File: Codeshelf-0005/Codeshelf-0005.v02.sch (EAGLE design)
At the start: 26 parts, among them J1 RJ45-8PTH, J2 RJ45-8PTH, U2 MC9S08QG-DT, U3 CAT9552, U4 RS485SOIC, U7 7SEGMENT-2DIGIT

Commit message: Changes related to design review with Ravi and Charlie.
Mainly we need a new way to connect all of the boards where the cables
enter the back.
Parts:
- removed ACK.BUTTON.KEYCAP, CASE, STANDOFF1, STANDOFF2, STANDOFF3, STANDOFF4: EXTERNAL-COMPONENT, GW-devices:EXTERNAL-COMPONENT
- removed BDM: HEADER-3X2, GW-devices:HEADER-3X2
- removed R.D2A, R.D2B, R.D2C, R.D2D: RESISTOR-ARRAY-4X-3216, GW-devices:RESISTOR-ARRAY-4X-3216
- removed SW-ACK: SWITCH-TACTILE-320.03E11, GW-devices:SWITCH-TACTILE-320.03E11
- removed SW-DEC, SW-INC: SWITCH-TACTILE-FSM, GW-devices:SWITCH-TACTILE-FSM
- removed U7: 7SEGMENT-2DIGIT, GW-devices:7SEGMENT-2DIGIT
- added C10: 10uF, SparkFun:CAP_POL1206
- added C11: 68uF, SparkFun:CAP_POL3528
- added C3, C4: 100pF, GW-devices:RF-C0603
- added C5, C6, C7, C8, C9: .1uF, GW-devices:RF-C0402
- added CCOMP: 68pF, GW-devices:RF-C0805
- added CIN: 47uF, GW-devices:RF-C1210
- added COUT1: 100uF, GW-devices:RF-C1210
- added CSS: 2.7nF, GW-devices:RF-C0805
- added D1: RED, led:LEDCHIP-LED0805
- added D2: GREEN, led:LEDCHIP-LED0805
- added D3: MBRA140, SparkFun:DIODESMA
- added J3-WAKE: M02PTH, SparkFun-Connectors:M02PTH
- added J4: RJ45-8PTH, SparkFun:RJ45-8PTH
- added J5: HEADER-2X-2.54MM, GW-devices:HEADER-2X-2.54MM
- added J5-LCD-3V3, J6-LCD-5V: (no value), SparkFun-Connectors:M03PTH
- added JF1, JF2: JUMPER-2X-SMT-VIA, GW-devices:JUMPER-2X-SMT-VIA
- added L1: 150uH, GW-devices:INDUCTOR-SMD-UNUSUAL-SLF10165
- added L2: 47uH, SparkFun:INDUCTORCR54
- added LCD: LCD-SPARKFUN, GW-devices:LCD-SPARKFUN20X4
- added LED-ACTION: LED5060A, GW-devices:LED5060A
- added R-T: 120, GW-devices:RF-R0402
- added R.ACT.B, R.ACT.G: 10, GW-devices:RF-R0402
- added R.ACT.R: 68, GW-devices:RF-R0402
- added RCOMP: 4.64K, GW-devices:RF-R0402
- added REN1: 22K, GW-devices:RF-R0402
- added REN2: 10K, GW-devices:RF-R0402
- added RFB1: 45.3K, GW-devices:RF-R0402
- added RFB2: 143K, GW-devices:RF-R0402
- added U-P1: LM2854MH, GW-devices:LM2854MH
- added U-P2: PCHANNEL-MOSFET-DPAK, GW-devices:PCHANNEL-MOSFET-DPAK
- added U-P3: NCP1402, SparkFun:V_REG_NCP1400SOT23-5
- added U1: ZSFM201-1A, GW-devices:ZSFM201-1A
- added U5, U6: MIC94061C6, GW-devices:MIC94061C6
- C1: value .1uF -> 100pF; device GW-devices:RF-C0402 -> GW-devices:RF-C0603; MFGP GRM033R61A104KE15D -> C0603C101K5RACTU; PRICE 0.02 -> (none)
- C2: value .1uF -> 1nF; device GW-devices:RF-C0402 -> GW-devices:RF-C0603; MFGP GRM033R61A104KE15D -> C0603C102K4RACTU; PRICE 0.02 -> (none)
- J1: value RJ45-8PTH -> M05X2PTH; device GW-devices:RJ45-8PTH -> SparkFun:M05X2PTH; MFGN FCI -> (none); MFGP 54602-908LF -> (none); PRICE 0.02 -> (none)
- J2: device GW-devices:RJ45-8PTH -> SparkFun:RJ45-8PTH
- R1: value 3.3K -> 100K; MFGP ERJ-2GEJ332X -> ERJ-2GEJ104X; PRICE 0.02 -> (none)
- R2: value 10K -> 220; MFGP ERJ-2GEJ332X -> ERJ-2GEJ224X; NOTES (none) -> DNP; PRICE 0.02 -> (none)
- R3: value 10K -> 390; MFGP ERJ-2GEJ332X -> ERJ-2GEJ394X; NOTES (none) -> DNP; PRICE 0.02 -> (none)
- U2: value MC9S08QG-DT -> MAX232SOIC16; device GW-devices:MC9S08QG-DT -> SparkFun:MAX232SOIC16; MFGN Freescale -> TI; MFGP MC9S08QG8CDTER -> MAX232DR; PRICE 1.73 -> 0.86
- U3: value CAT9552 -> RS485SOIC; device GW-devices:CAT9552 -> SparkFun:RS485SOIC; MFGN (none) -> TI; MFGP (none) -> SN65HVD1781DR; PRICE (none) -> 3.86
- U4: value RS485SOIC -> ULN2003AD; device SparkFun:RS485SOIC -> uln-udn:ULN2003AD; MFGP SN65HVD1781DR -> ULN2003ADR; PRICE 4.29 -> 0.18
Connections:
- removed net N$27: R.D2C.3B, U7.1D
- removed net N$29: R.D2B.1A, U7.1DP
- removed net N$31: R.D2D.4A, U3.LED8
- removed net N$32: R.D2D.3A, U3.LED9
- removed net RS485_N: J1.4, J2.4, U4.B
- removed net RS485_P: J1.5, J2.5, U4.A
- removed net RX: U2.PTB0/RX, U4.RO
- removed net SLA: R2.1, U2.PTA2/KBIP2, U3.SDA
- removed net SLC: R3.1, U2.PTA3, U3.SCL
- removed net TX: U2.PTB1/TX, U4.DI
- new net +5V: C11.+, D3.C, J2.2, U-P3.EN, U-P3.OUT, U5.VIN
- new net C1: C5.1, U2.C1+
- new net C2: C6.1, U2.C2+
- new net N$39: U1.TMR2/10, U4.I3
- new net R1IN: J2.4, U2.R1IN
- new net R1OUT: U1.UART1_RX, U2.R1OUT
- new net RTCK: J1.4, U1.RTCK
- new net T1IN: J5-LCD-3V3.2, U1.UART1_TX, U2.T1IN
- new net T1OUT: J6-LCD-5V.2, U2.T1OUT
- new net TCK: J1.3, U1.TCK
- new net TDI: J1.5, U1.TDI
- new net TDO: J1.7, U1.TDO
- new net TMS: J1.1, U1.TMS
- new net V-PROT: CIN.1, REN1.2, U-P1.AVIN, U-P1.PVIN5, U-P1.PVIN6, U-P1.PVIN7, U-P2.S
- new net VBATT: J5.2, U-P2.D
- net +3V3: now also C10.+, C3.2, C4.2, C9.1, CCOMP.2, COUT1.1, J1.9, J4.1, JF1.1, L1.2, L2.1, LED-ACTION.B+, LED-ACTION.G+, LED-ACTION.R+, RFB2.2, U1.LREG, U1.VCC1, U1.VCC2, U2.VCC, U6.VIN; no longer BDM.6, J1.1, J2.1, R2.2, R3.2, U2.VDD, U4.VCC, U7.G1, U7.G2
- net GND: now also C10.-, C11.-, C2.2, C3.1, C4.1, C7.2, C8.2, C9.2, CIN.2, COUT1.2, CSS.2, J1.10, J2.3, J4.8, J5-LCD-3V3.1, J5.1, J6-LCD-5V.1, JF2.1, R2.1, R3.1, REN2.1, RFB1.1, U-P1.AGND, U-P1.EXP, U-P1.NC1, U-P1.NC8, U-P1.NC9, U-P1.PGND2, U-P1.PGND3, U-P1.PGND4, U-P2.G, U-P3.GND, U1.GND1, U1.GND2, U1.GND3, U1.GND4, U1.GND5, U1.GND6, U1.GND7, U1.GND8, U1.GND9, U2.GND, U5.GND1, U5.GND2, U6.GND1, U6.GND2; no longer BDM.2, C2.1, J1.8, J2.8, SW-ACK.3, SW-ACK.4, SW-DEC.3, SW-DEC.4, SW-INC.3, SW-INC.4, U2.VSS, U3.A0, U3.A1, U3.A2
- net N$1: now also D2.A, U1.KBI0; no longer R.D2A.4B, U3.LED7
- net N$10: now also J5-LCD-3V3.3, U6.VOUT; no longer R.D2B.3B, U3.LED2
- net N$11: now also C6.2, U2.C2-; no longer R.D2B.2B, U3.LED1
- net N$12: now also C7.1, U2.V-; no longer R.D2B.1B, U3.LED0
- net N$13: now also J6-LCD-5V.3, U5.VOUT; no longer R.D2D.1B, U7.2DP
- net N$14: now also J3-WAKE.2, U1.KBI7; no longer R.D2D.2B, U7.2C
- net N$15: now also C8.1, U2.V+; no longer R.D2D.3B, U7.2D
- net N$16: now also J3-WAKE.1, U1.KBI4; no longer R.D2D.4B, U7.2E
- net N$17: now also U1.UART2_TX, U3.DI; no longer R.D2A.1A, U7.2B
- net N$18: now also U1.UART2_RX, U3.RO; no longer R.D2A.2A, U7.2A
- net N$19: now also U1.UART2_RTS, U3./RE, U3.DE; no longer U2.PTB3, U4./RE, U4.DE
- net N$2: now also D1.A, U1.KBI1; no longer R.D2A.3B, U3.LED6
- net N$20: now also J4.4, R-T.1, U3.B; no longer R.D2A.3A, U7.2G
- net N$21: now also J4.5, R-T.2, U3.A; no longer R.D2A.4A, U7.2F
- net N$22: now also CSS.1, U-P1.SS; no longer R.D2B.4A, U7.1F
- net N$23: now also L1.1, U-P1.SW12, U-P1.SW13; no longer BDM.4, C2.2, U2.PTA5/RESET
- net N$24: now also RCOMP.2, RFB1.2, RFB2.1, U-P1.FB; no longer R.D2B.3A, U7.1A
- net N$25: now also CCOMP.1, RCOMP.1; no longer R.D2C.1B, U7.1C
- net N$26: now also REN1.1, REN2.2, U-P1.EN; no longer R.D2C.2B, U7.1G
- net N$28: now also R.ACT.R.2, U4.O2; no longer R.D2C.4B, U7.1E
- net N$3: now also D2.C, R3.2; no longer R.D2A.2B, U3.LED5
- net N$30: now also R.ACT.G.2, U4.O3; no longer R.D2B.2A, U7.1B
- net N$33: now also LED-ACTION.B-, R.ACT.B.1; no longer R.D2D.2A, U3.LED10
- net N$34: now also LED-ACTION.R-, R.ACT.R.1; no longer R.D2D.1A, U3.LED11
- net N$35: now also LED-ACTION.G-, R.ACT.G.1; no longer R.D2C.4A, U3.LED12
- net N$36: now also U1.TMR0/8, U4.I1; no longer R.D2C.3A, U3.LED13
- net N$37: now also U1.TMR1/9, U4.I2; no longer R.D2C.2A, U3.LED14
- net N$38: now also R.ACT.B.2, U4.O1; no longer R.D2C.1A, U3.LED15
- net N$4: now also D1.C, R2.2; no longer R.D2A.1B, U3.LED4
- net N$5: now also D3.A, L2.2, U-P3.LX; no longer R.D2B.4B, U3.LED3
- net N$6: now also JF2.2, U1.ADC2_VREFH; no longer SW-ACK.1, SW-ACK.2, U2.PTA0/KBIP0
- net N$7: now also JF1.2, U1.ADC2_VREFL; no longer SW-DEC.1, SW-DEC.2, U2.PTA1/KBIP1
- net N$8: now also C5.2, U2.C1-; no longer SW-INC.1, SW-INC.2, U2.PTB2
- net N$9: now also U1.I2C_SDA, U5.EN, U6.EN; no longer BDM.1, R1.1, U2.PTA4/BDM
- net RESET: now also C2.1, J1.2, R1.1, U1.RESETB; no longer U2.PTB5, U3.#RESET
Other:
- note added: "Consider removing 5V from the circuit since the barcode scanner seems to work at 3.3v"

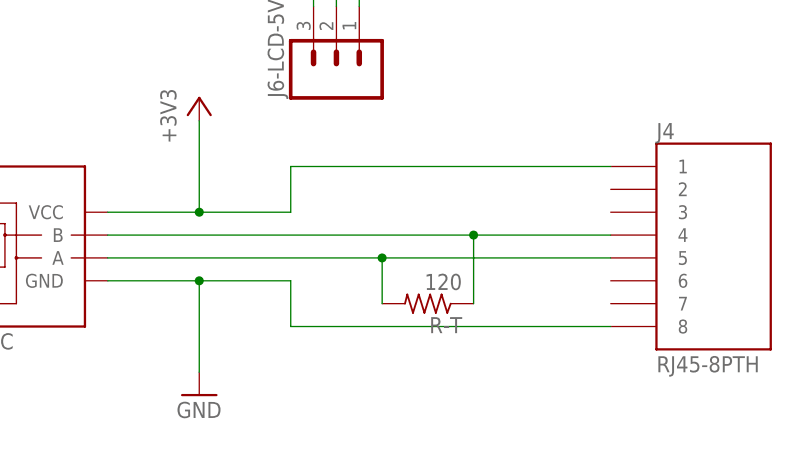
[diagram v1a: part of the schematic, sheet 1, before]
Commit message: CHE controller changes for Ravi & Charlie feedback
RS485 3V/GND on two conductors
Scanner pins separated from RS485 pins on EN patch cables.
Sleep switch and power control of scanner the LCD display
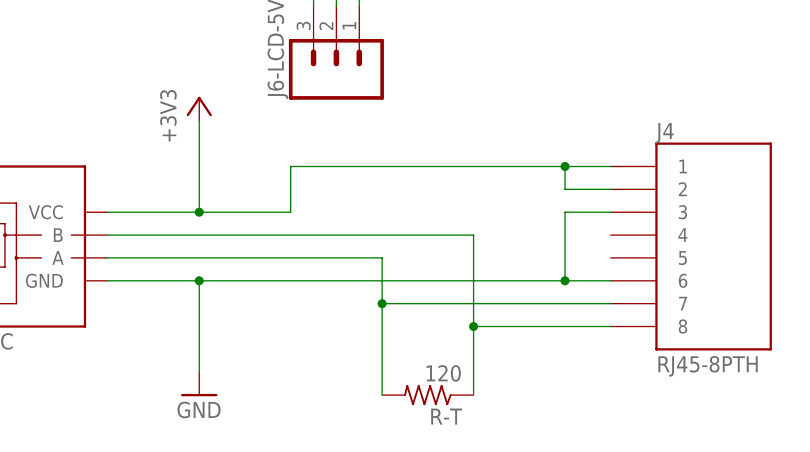
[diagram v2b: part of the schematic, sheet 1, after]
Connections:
- net +3V3: now also J4.2
- net GND: now also J4.3, J4.6; no longer J4.8
- net N$20: now also J4.8; no longer J4.4
- net N$21: now also J4.7; no longer J4.5
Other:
- moved on the sheet: R-T
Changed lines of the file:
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@@
 <attribute name="PRICE" x="88.9" y="-124.46" size="1.778" layer="96" display="off"/>
 </instance>
-<instance part="R-T" gate="G$1" x="139.7" y="-132.08" rot="R180">
-<attribute name="MFGN" x="139.7" y="-132.08" size="1.778" layer="96" rot="R180" display="off"/>
-<attribute name="MFGP" x="139.7" y="-132.08" size="1.778" layer="96" rot="R180" display="off"/>
-<attribute name="PRICE" x="139.7" y="-132.08" size="1.778" layer="96" rot="R180" display="off"/>
+<instance part="R-T" gate="G$1" x="139.7" y="-142.24" rot="R180">
+<attribute name="MFGN" x="139.7" y="-142.24" size="1.778" layer="96" rot="R180" display="off"/>
+<attribute name="MFGP" x="139.7" y="-142.24" size="1.778" layer="96" rot="R180" display="off"/>
+<attribute name="PRICE" x="139.7" y="-142.24" size="1.778" layer="96" rot="R180" display="off"/>
 </instance>
 <instance part="JF1" gate="G$1" x="-73.66" y="20.32"/>
@@
 <wire x1="104.14" y1="-129.54" x2="114.3" y2="-129.54" width="0.1524" layer="91"/>
 <wire x1="114.3" y1="-129.54" x2="114.3" y2="-139.7" width="0.1524" layer="91"/>
-<wire x1="114.3" y1="-129.54" x2="124.46" y2="-129.54" width="0.1524" layer="91"/>
-<wire x1="124.46" y1="-129.54" x2="124.46" y2="-134.62" width="0.1524" layer="91"/>
-<wire x1="124.46" y1="-134.62" x2="160.02" y2="-134.62" width="0.1524" layer="91"/>
 <junction x="114.3" y="-129.54"/>
 <pinref part="GND8" gate="1" pin="GND"/>
-<pinref part="J4" gate="G$1" pin="8"/>
 <pinref part="U3" gate="G$1" pin="GND"/>
+<pinref part="J4" gate="G$1" pin="6"/>
+<wire x1="114.3" y1="-129.54" x2="154.94" y2="-129.54" width="0.1524" layer="91"/>
+<pinref part="J4" gate="G$1" pin="3"/>
+<wire x1="154.94" y1="-129.54" x2="160.02" y2="-129.54" width="0.1524" layer="91"/>
+<wire x1="160.02" y1="-121.92" x2="154.94" y2="-121.92" width="0.1524" layer="91"/>
+<wire x1="154.94" y1="-121.92" x2="154.94" y2="-129.54" width="0.1524" layer="91"/>
+<junction x="154.94" y="-129.54"/>
 </segment>
 <segment>
@@
 </segment>
 </net>
-<net name="+3V3" class="1">
+<net name="+3V3" class="0">
 <segment>
 <wire x1="-48.26" y1="-20.32" x2="-60.96" y2="-20.32" width="0.1524" layer="91"/>
@@
 <wire x1="114.3" y1="-121.92" x2="124.46" y2="-121.92" width="0.1524" layer="91"/>
 <wire x1="124.46" y1="-121.92" x2="124.46" y2="-116.84" width="0.1524" layer="91"/>
-<wire x1="124.46" y1="-116.84" x2="160.02" y2="-116.84" width="0.1524" layer="91"/>
+<wire x1="124.46" y1="-116.84" x2="154.94" y2="-116.84" width="0.1524" layer="91"/>
 <junction x="114.3" y="-121.92"/>
 <pinref part="+3V8" gate="G$1" pin="+3V3"/>
 <pinref part="J4" gate="G$1" pin="1"/>
 <pinref part="U3" gate="G$1" pin="VCC"/>
+<pinref part="J4" gate="G$1" pin="2"/>
+<wire x1="154.94" y1="-116.84" x2="160.02" y2="-116.84" width="0.1524" layer="91"/>
+<wire x1="160.02" y1="-119.38" x2="154.94" y2="-119.38" width="0.1524" layer="91"/>
+<wire x1="154.94" y1="-119.38" x2="154.94" y2="-116.84" width="0.1524" layer="91"/>
+<junction x="154.94" y="-116.84"/>
 </segment>
 <segment>
@@
 </segment>
 </net>
-<net name="+5V" class="2">
+<net name="+5V" class="0">
 <segment>
 <wire x1="231.14" y1="5.08" x2="231.14" y2="17.78" width="0.1524" layer="91"/>
@@
 <segment>
 <wire x1="104.14" y1="-124.46" x2="144.78" y2="-124.46" width="0.1524" layer="91"/>
-<wire x1="144.78" y1="-124.46" x2="160.02" y2="-124.46" width="0.1524" layer="91"/>
-<wire x1="144.78" y1="-132.08" x2="144.78" y2="-124.46" width="0.1524" layer="91"/>
-<junction x="144.78" y="-124.46"/>
-<pinref part="J4" gate="G$1" pin="4"/>
+<wire x1="144.78" y1="-142.24" x2="144.78" y2="-134.62" width="0.1524" layer="91"/>
 <pinref part="U3" gate="G$1" pin="B"/>
 <pinref part="R-T" gate="G$1" pin="1"/>
+<pinref part="J4" gate="G$1" pin="8"/>
+<wire x1="144.78" y1="-134.62" x2="144.78" y2="-124.46" width="0.1524" layer="91"/>
+<wire x1="160.02" y1="-134.62" x2="144.78" y2="-134.62" width="0.1524" layer="91"/>
+<junction x="144.78" y="-134.62"/>
 </segment>
 </net>
@@
 <segment>
 <wire x1="104.14" y1="-127" x2="134.62" y2="-127" width="0.1524" layer="91"/>
-<wire x1="134.62" y1="-127" x2="160.02" y2="-127" width="0.1524" layer="91"/>
-<wire x1="134.62" y1="-132.08" x2="134.62" y2="-127" width="0.1524" layer="91"/>
-<junction x="134.62" y="-127"/>
-<pinref part="J4" gate="G$1" pin="5"/>
+<wire x1="134.62" y1="-142.24" x2="134.62" y2="-132.08" width="0.1524" layer="91"/>
 <pinref part="U3" gate="G$1" pin="A"/>
 <pinref part="R-T" gate="G$1" pin="2"/>
+<pinref part="J4" gate="G$1" pin="7"/>
+<wire x1="134.62" y1="-132.08" x2="134.62" y2="-127" width="0.1524" layer="91"/>
+<wire x1="160.02" y1="-132.08" x2="134.62" y2="-132.08" width="0.1524" layer="91"/>
+<junction x="134.62" y="-132.08"/>
 </segment>
 </net>
@@
 </segment>
 </net>
-<net name="+3V3" class="1">
+<net name="+3V3" class="0">
 <segment>
 <wire x1="535.94" y1="60.96" x2="546.1" y2="60.96" width="0.1524" layer="91"/>
@@
 </segment>
 </net>
-<net name="+3V3" class="1">
+<net name="+3V3" class="0">
 <segment>
 <wire x1="393.7" y1="-99.06" x2="388.62" y2="-99.06" width="0.1524" layer="91"/>
@@
 </segment>
 </net>
-<net name="+5V" class="2">
+<net name="+5V" class="0">
 <segment>
 <wire x1="434.34" y1="-99.06" x2="436.88" y2="-99.06" width="0.1524" layer="91"/>

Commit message: BOM review before first articles of 0005, 0007, 0008, 0012
Reviewed BOM with Charlie
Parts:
- C1, C2, C3, C4: MFGN Murata -> Kemet
- LED-ACTION: MFGN (none) -> BiVar; MFGP (none) -> SMP6-RGB
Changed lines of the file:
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@@
 <part name="J1" library="SparkFun" deviceset="M05X2" device="PTH"/>
 <part name="C1" library="GW-devices" deviceset="RF-C" device="0603" value="100pF">
-<attribute name="MFGN" value="Murata"/>
+<attribute name="MFGN" value="Kemet"/>
 <attribute name="MFGP" value="C0603C101K5RACTU"/>
 </part>
 <part name="C2" library="GW-devices" deviceset="RF-C" device="0603" value="1nF">
-<attribute name="MFGN" value="Murata"/>
+<attribute name="MFGN" value="Kemet"/>
 <attribute name="MFGP" value="C0603C102K4RACTU"/>
 </part>
@@
 </part>
 <part name="C3" library="GW-devices" deviceset="RF-C" device="0603" value="100pF">
-<attribute name="MFGN" value="Murata"/>
+<attribute name="MFGN" value="Kemet"/>
 <attribute name="MFGP" value="C0603C101K5RACTU"/>
 </part>
 <part name="C4" library="GW-devices" deviceset="RF-C" device="0603" value="100pF">
-<attribute name="MFGN" value="Murata"/>
+<attribute name="MFGN" value="Kemet"/>
 <attribute name="MFGP" value="C0603C101K5RACTU"/>
 </part>
@@
 </part>
 <part name="LCD" library="GW-devices" deviceset="LCD-SPARKFUN" device="20X4" value="LCD-SPARKFUN"/>
-<part name="LED-ACTION" library="GW-devices" deviceset="LED5060" device="A"/>
+<part name="LED-ACTION" library="GW-devices" deviceset="LED5060" device="A">
+<attribute name="MFGN" value="BiVar"/>
+<attribute name="MFGP" value="SMP6-RGB"/>
+</part>
 <part name="U4" library="uln-udn" deviceset="ULN2003A" device="D">
 <attribute name="MFGN" value="TI"/>
@@
 </instance>
 <instance part="LCD" gate="G$1" x="259.08" y="83.82"/>
-<instance part="LED-ACTION" gate="G$1" x="149.86" y="99.06" rot="R270"/>
+<instance part="LED-ACTION" gate="G$1" x="149.86" y="99.06" rot="R270">
+<attribute name="MFGN" x="149.86" y="99.06" size="1.778" layer="96" rot="R270" display="off"/>
+<attribute name="MFGP" x="149.86" y="99.06" size="1.778" layer="96" rot="R270" display="off"/>
+</instance>
 <instance part="U4" gate="A" x="114.3" y="129.54">
 <attribute name="MFGN" x="114.3" y="129.54" size="1.778" layer="96" display="off"/>

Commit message: Remove 5V SMPS
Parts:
- removed C10: 10uF, SparkFun:CAP_POL1206
- removed C11: 68uF, SparkFun:CAP_POL3528
- removed D3: MBRA140, SparkFun:DIODESMA
- removed J6-LCD-5V: (no value), SparkFun-Connectors:M03PTH
- removed L2: 47uH, SparkFun:INDUCTORCR54
- removed U-P3: NCP1402, SparkFun:V_REG_NCP1400SOT23-5
- removed U5: MIC94061C6, GW-devices:MIC94061C6
- J5: value HEADER-2X-2.54MM -> (none); device GW-devices:HEADER-2X-2.54MM -> pinhead:PINHD-1X2/90
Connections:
- removed net +5V: C11.+, D3.C, J2.2, U-P3.EN, U-P3.OUT, U5.VIN
- removed net N$13: J6-LCD-5V.3, U5.VOUT
- removed net N$5: D3.A, L2.2, U-P3.LX
- removed net T1OUT: J6-LCD-5V.2, U2.T1OUT
- net +3V3: now also J2.2; no longer C10.+, L2.1
- net GND: no longer C10.-, C11.-, J6-LCD-5V.1, U-P3.GND, U5.GND1, U5.GND2
- net N$9: no longer U5.EN
